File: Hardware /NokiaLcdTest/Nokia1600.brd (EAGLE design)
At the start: 38 x 66 mm, 9 parts

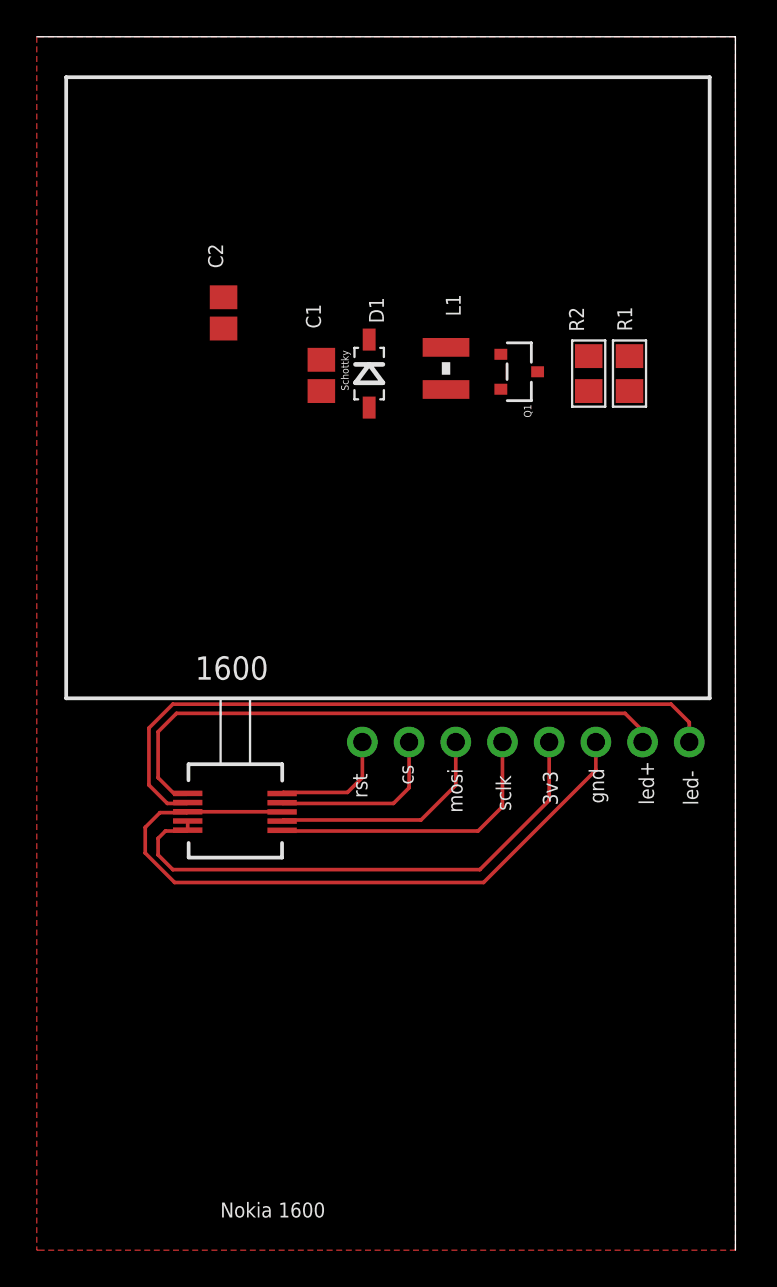
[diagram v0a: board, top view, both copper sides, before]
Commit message: Trabajo en desarrollo CenditLab + hardware Cendit11713
   - Modulo Task, se crea clases para menejo de Instrumentos (Instrument)
   - Ediciones de esquematicos Cendit11714 + tarjeta Nokia 1600 LCD
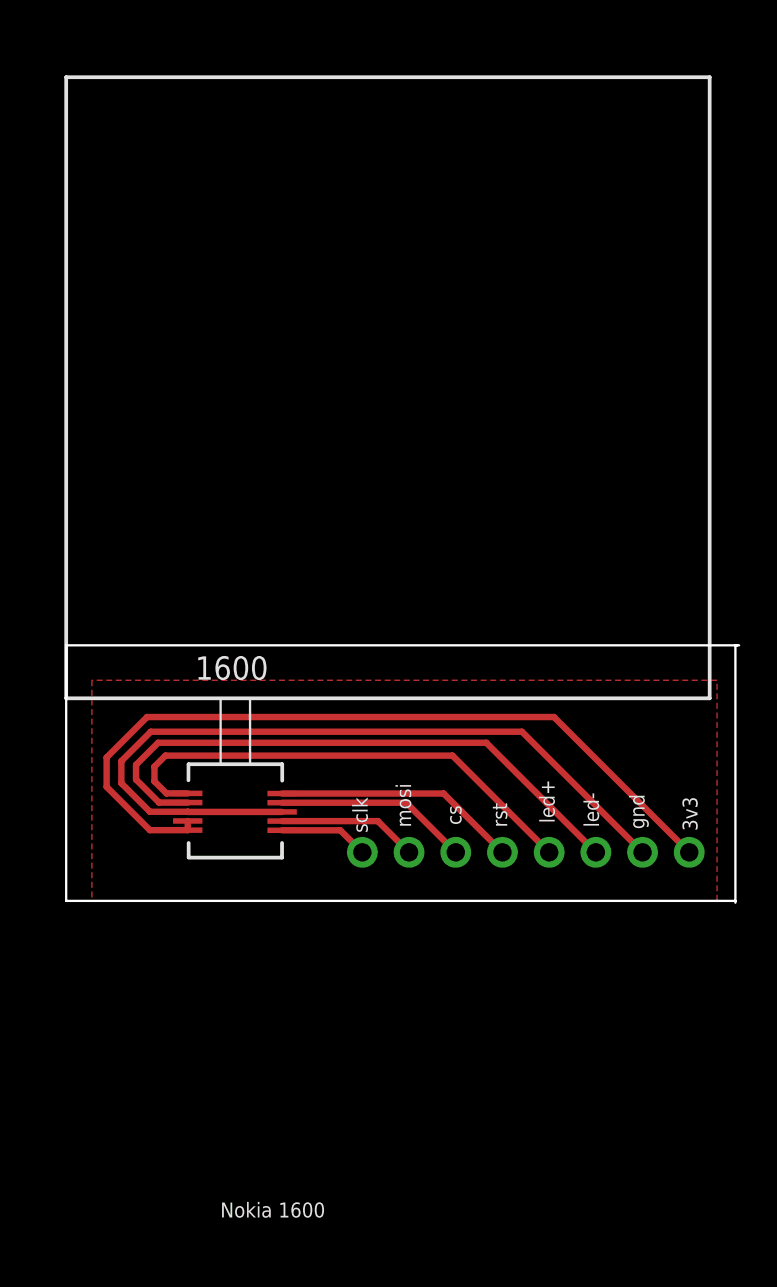
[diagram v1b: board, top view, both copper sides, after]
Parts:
- removed C1: 4.7uf, adafruit:C0805
- removed C2: 1uf, adafruit:C0805
- removed D1: Schottky, microbuilder:SOD-123
- removed L1: (no value), PeterAtMega644:WE-KI_1008_B
- removed Q1: (no value), microbuilder:SOT23-R
- removed R1: 10, microbuilder:0805
- removed R2: 4k7, microbuilder:0805
- moved JP1 6.00 mm to (26.6, 21.6)
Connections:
- removed net N$6: D1.A, L1.2, Q1.3
- removed net PWRPWM: Q1.1, R2.2
- net CLK: now also JP1.1; no longer JP1.4
- net CS: now also JP1.3; no longer JP1.2
- net GND: now also JP1.7; no longer C1.2, C2.2, JP1.6, Q1.2, R1.1, R2.1
- net LED+: now also JP1.5; no longer C2.1, D1.C, JP1.7
- net LED-: now also JP1.6; no longer JP1.8, R1.2
- net RESET: now also JP1.4; no longer JP1.1
- net SDA: now also JP1.2; no longer JP1.3
- net VCC: now also JP1.8; no longer C1.1, JP1.5, L1.1
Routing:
- net VCC: track 29.5 -> 43.1 mm
- net CLK: track 16.1 -> 4.86 mm
- net RESET: track 6.66 -> 13.3 mm
- net LED+: track 32.3 -> 26.8 mm
- net SDA: track 12.6 -> 7.61 mm
- net LED-: track 37.1 -> 32.1 mm
- net GND: track 38.4 -> 42.3 mm
- net CS: track 9.76 -> 10.6 mm
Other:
- board size 38 x 66 mm -> 36.6 x 14 mm

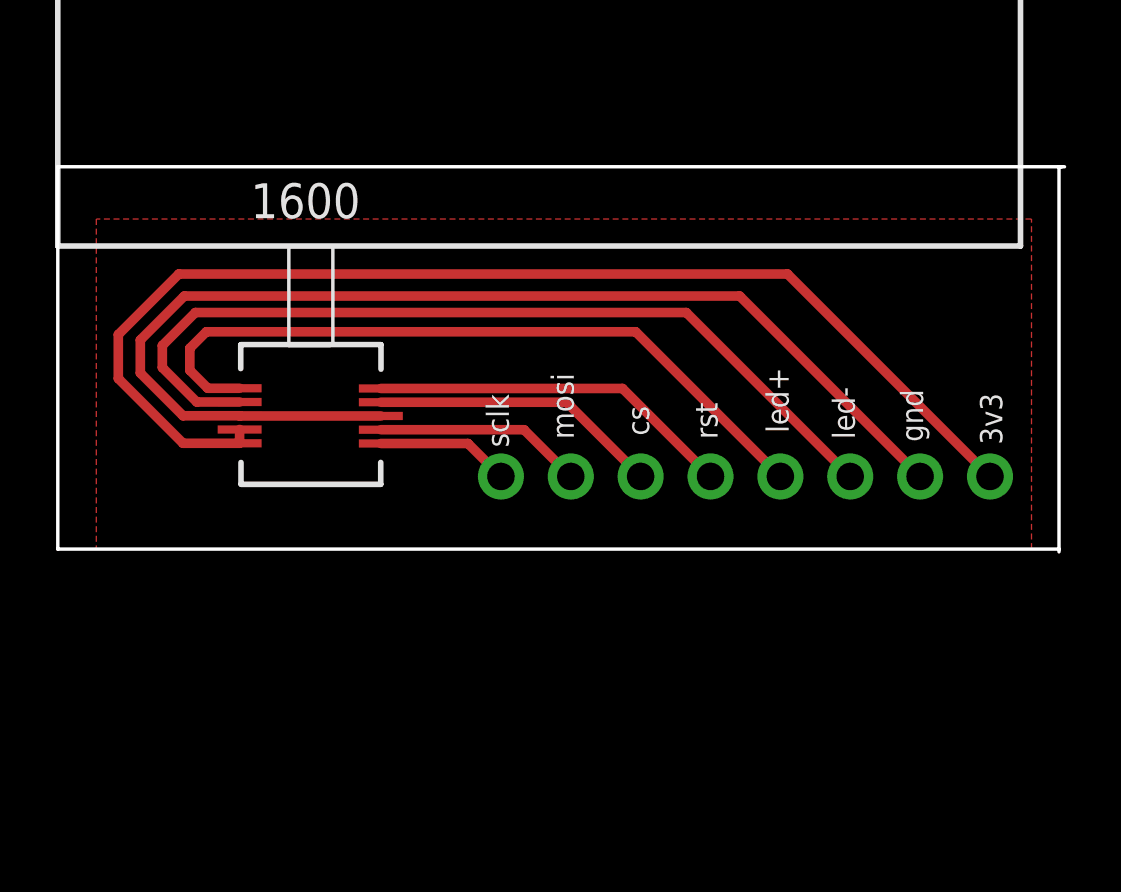
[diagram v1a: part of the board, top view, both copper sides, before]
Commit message: Trabajo en Cenditlab + Tarjeta pantalla Nokia
  - En CenditLab trabajo en contenedor de datos para graficos GraphData
  - Instalador basico, v0.4
  - PCB para LCD nokia 1600 se agrega card header
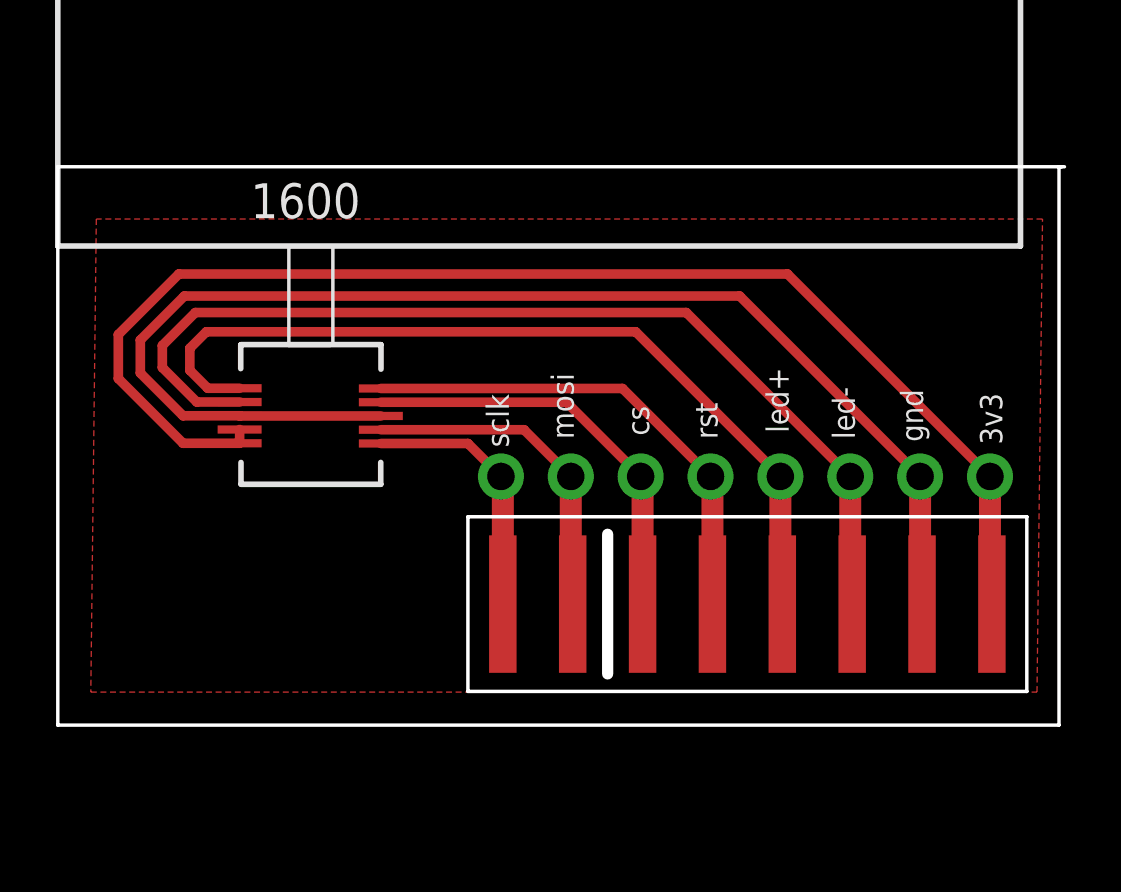
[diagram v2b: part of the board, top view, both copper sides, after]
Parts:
- added EDGE1: CARD-EDGE-8P, SistemaCendit11713v2:DUOPLUG-8P-KEYED
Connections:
- net CLK: now also EDGE1.1
- net CS: now also EDGE1.3
- net GND: now also EDGE1.7
- net LED+: now also EDGE1.5
- net LED-: now also EDGE1.6
- net RESET: now also EDGE1.4
- net SDA: now also EDGE1.2
- net VCC: now also EDGE1.8
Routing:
- net VCC: track 43.1 -> 47.8 mm
- net SDA: track 7.61 -> 12.3 mm
- net LED-: track 32.1 -> 36.8 mm
- net LED+: track 26.8 -> 31.5 mm
- net GND: track 42.3 -> 47.0 mm
- net CS: track 10.6 -> 15.3 mm
- net CLK: track 4.86 -> 9.57 mm
- net RESET: track 13.3 -> 17.4 mm
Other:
- board size 36.6 x 14 mm -> 36.6 x 20.3 mm
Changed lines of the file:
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@@
 <?xml version="1.0" encoding="utf-8"?>
 <!DOCTYPE eagle SYSTEM "eagle.dtd">
-<eagle version="7.7.0">
+<eagle version="7.2.0">
 <drawing>
 <settings>
@@
 <layer number="54" name="bGND_GNDA" color="1" fill="9" visible="no" active="no"/>
 <layer number="56" name="wert" color="7" fill="1" visible="no" active="yes"/>
+<layer number="90" name="Modules" color="5" fill="1" visible="no" active="no"/>
 <layer number="91" name="Nets" color="2" fill="1" visible="no" active="no"/>
 <layer number="92" name="Busses" color="1" fill="1" visible="no" active="no"/>
@@
 <text x="9.98" y="1.78" size="0.8128" layer="21">Nokia 1600
 </text>
-<wire x1="1.6" y1="32.9" x2="1.6" y2="19" width="0.125" layer="20"/>
-<wire x1="1.6" y1="19" x2="38" y2="19" width="0.125" layer="20"/>
+<wire x1="1.6" y1="32.9" x2="1.6" y2="12.6" width="0.125" layer="20"/>
+<wire x1="1.6" y1="12.6" x2="38" y2="12.6" width="0.125" layer="20"/>
 <wire x1="1.6" y1="32.9" x2="38.1" y2="32.9" width="0.125" layer="20"/>
 <wire x1="38.2" y1="32.9" x2="38" y2="32.9" width="0.125" layer="20"/>
-<wire x1="38" y1="32.9" x2="38" y2="19" width="0.125" layer="20"/>
-<wire x1="38" y1="19" x2="38" y2="18.9" width="0.125" layer="20"/>
+<wire x1="38" y1="32.9" x2="38" y2="12.6" width="0.125" layer="20"/>
 </plain>
 <attributes>
@@
 </element>
 <element name="U$1" library="PeterAtMega644" package="NOKIA1600_LCD" value="NOKIA1600_LCD" x="36.6" y="63.8" rot="R180"/>
+<element name="EDGE1" library="SistemaCendit11713v2" package="DUOPLUG-8P-KEYED" value="CARD-EDGE-8P" x="25.4" y="17" smashed="yes" rot="R90">
+<attribute name="NAME" x="15.075" y="14.025" size="0.6096" layer="27" rot="R90"/>
+<attribute name="VALUE" x="16.135" y="14.425" size="0.6096" layer="27" rot="R90"/>
+</element>
 </elements>
 <signals>
@@
 <contactref element="U$1" pad="3"/>
 <contactref element="U$1" pad="8"/>
-<polygon width="0.125" layer="1" isolate="0.5" orphans="yes">
-<vertex x="3" y="19"/>
-<vertex x="37" y="19"/>
-<vertex x="37" y="31"/>
+<polygon width="0.2" layer="1" isolate="1.2" orphans="yes">
+<vertex x="2.8" y="13.8"/>
+<vertex x="37.2" y="13.8"/>
+<vertex x="37.4" y="31"/>
 <vertex x="3" y="31"/>
 </polygon>
@@
 <wire x1="13.3446" y1="23.839" x2="8.2186" y2="23.839" width="0.35" layer="1"/>
 <wire x1="8.2186" y1="23.839" x2="8.2106" y2="23.847" width="0.35" layer="1"/>
+<contactref element="EDGE1" pad="7"/>
+<wire x1="33.02" y1="17" x2="32.95" y2="17" width="0.8" layer="1"/>
+<wire x1="32.95" y1="17" x2="32.95" y2="21.64" width="0.8" layer="1"/>
 </signal>
 <signal name="VCC" class="1">
@@
 <wire x1="6" y1="29" x2="28.13" y2="29" width="0.35" layer="1"/>
 <wire x1="28.13" y1="29" x2="35.49" y2="21.64" width="0.35" layer="1"/>
+<contactref element="EDGE1" pad="8"/>
+<wire x1="35.56" y1="17" x2="35.49" y2="17" width="0.8" layer="1"/>
+<wire x1="35.49" y1="17" x2="35.49" y2="21.64" width="0.8" layer="1"/>
 </signal>
 <signal name="LED+" class="1">
@@
 <wire x1="7" y1="26.9" x2="22.61" y2="26.9" width="0.35" layer="1"/>
 <wire x1="22.61" y1="26.9" x2="27.87" y2="21.64" width="0.35" layer="1"/>
+<contactref element="EDGE1" pad="5"/>
+<wire x1="27.94" y1="17" x2="27.87" y2="17" width="0.8" layer="1"/>
+<wire x1="27.87" y1="17" x2="27.87" y2="21.64" width="0.8" layer="1"/>
 </signal>
 <signal name="RESET">
@@
 <wire x1="13.3446" y1="24.839" x2="22.131" y2="24.839" width="0.35" layer="1"/>
 <wire x1="22.131" y1="24.839" x2="25.33" y2="21.64" width="0.35" layer="1"/>
+<contactref element="EDGE1" pad="4"/>
+<wire x1="25.33" y1="21.64" x2="25.4" y2="21.64" width="0.8" layer="1"/>
+<wire x1="25.4" y1="21.64" x2="25.4" y2="17.6" width="0.8" layer="1"/>
+<wire x1="25.4" y1="17.6" x2="25.4" y2="17" width="0" layer="19" extent="1-1"/>
 </signal>
 <signal name="SDA">
@@
 <wire x1="13.3446" y1="23.339" x2="18.551" y2="23.339" width="0.35" layer="1"/>
 <wire x1="18.551" y1="23.339" x2="20.25" y2="21.64" width="0.35" layer="1"/>
+<contactref element="EDGE1" pad="2"/>
+<wire x1="20.32" y1="17" x2="20.25" y2="17" width="0.8" layer="1"/>
+<wire x1="20.25" y1="17" x2="20.25" y2="21.64" width="0.8" layer="1"/>
 </signal>
 <signal name="CLK">
@@
 <wire x1="13.3446" y1="22.839" x2="16.511" y2="22.839" width="0.35" layer="1"/>
 <wire x1="16.511" y1="22.839" x2="17.71" y2="21.64" width="0.35" layer="1"/>
+<contactref element="EDGE1" pad="1"/>
+<wire x1="17.71" y1="21.64" x2="17.78" y2="21.64" width="0.8" layer="1"/>
+<wire x1="17.78" y1="21.64" x2="17.78" y2="17" width="0.8" layer="1"/>
 </signal>
 <signal name="CS">
@@
 <wire x1="13.3446" y1="24.339" x2="20.091" y2="24.339" width="0.35" layer="1"/>
 <wire x1="20.091" y1="24.339" x2="22.79" y2="21.64" width="0.35" layer="1"/>
+<contactref element="EDGE1" pad="3"/>
+<wire x1="22.79" y1="21.64" x2="22.86" y2="21.64" width="0.8" layer="1"/>
+<wire x1="22.86" y1="21.64" x2="22.86" y2="17" width="0.8" layer="1"/>
 </signal>
 <signal name="LED-">
@@
 <wire x1="6.6" y1="27.6" x2="24.45" y2="27.6" width="0.35" layer="1"/>
 <wire x1="24.45" y1="27.6" x2="30.41" y2="21.64" width="0.35" layer="1"/>
+<contactref element="EDGE1" pad="6"/>
+<wire x1="30.48" y1="17" x2="30.41" y2="17" width="0.8" layer="1"/>
+<wire x1="30.41" y1="17" x2="30.41" y2="21.64" width="0.8" layer="1"/>
 </signal>
 </signals>
